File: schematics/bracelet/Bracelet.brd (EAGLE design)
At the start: 70 x 25 mm, 14 parts

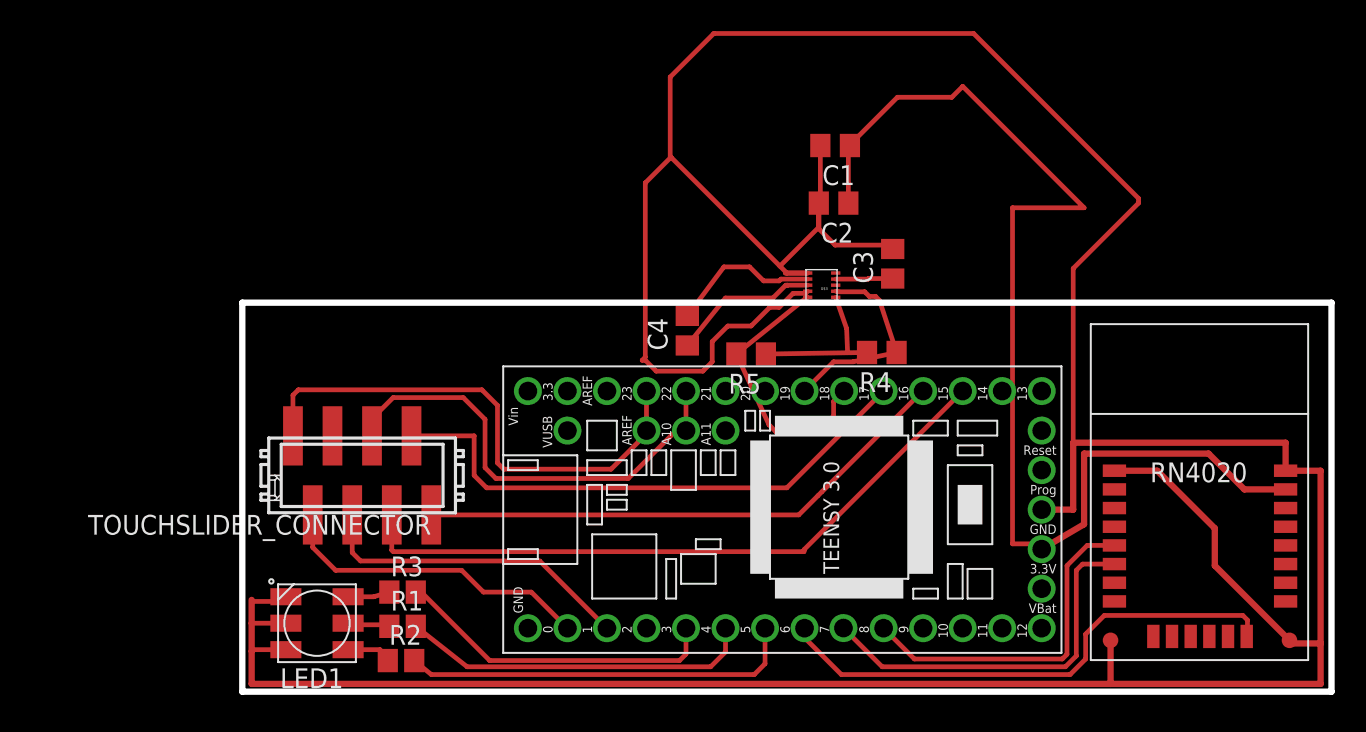
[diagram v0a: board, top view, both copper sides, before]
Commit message: finished layout, accel pullups need to be conf'ed to internal.
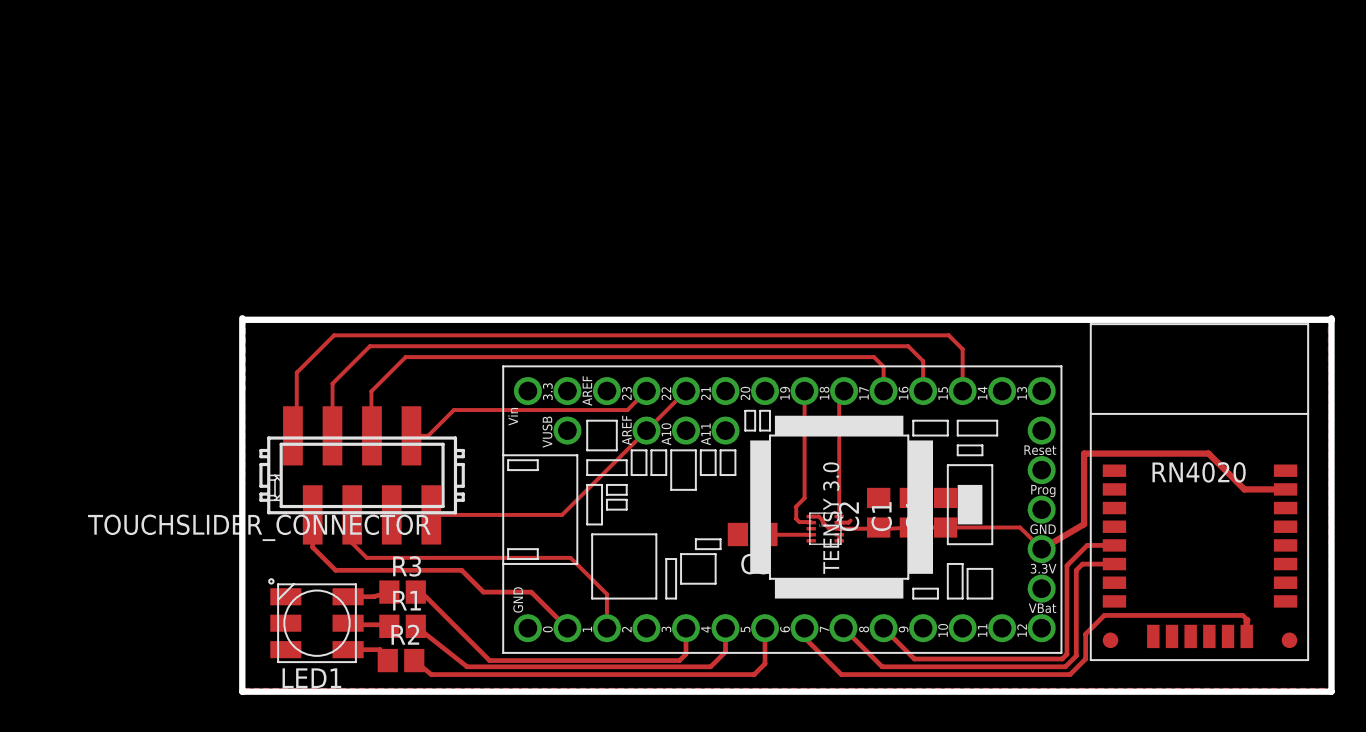
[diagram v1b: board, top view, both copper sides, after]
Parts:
- removed R4, R5: 1k, rcl:R0805
- moved C1 24.1 mm to (56.0, 36.5), turned to 90 degrees
- moved C4 20.3 mm to (58.2, 36.5)
- moved C2 20.1 mm to (53.9, 36.5), turned to 90 degrees
- moved C3 19.6 mm to (45.8, 35.1), turned to 180 degrees
- moved U$3 17.7 mm to (49.2, 34.5), turned to 0 degrees
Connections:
- removed net VDDIO: R4.2, R5.1
- net CAP01: now also U$1.P17; no longer U$1.P25
- net CAP03: now also U$1.P18
- net CAP05: now also U$1.P19; no longer U$1.P24
- net CAP06: no longer U$1.P17
- net CAP07: now also U$1.P25; no longer U$1.P19
- net CAP08: now also U$1.P24; no longer U$1.P18
- net SCL: no longer R4.1
- net SDA: no longer R5.2
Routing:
- net GND: track 265.8 -> 1.18 mm
- net +3V3: track 86.9 -> 37.7 mm
- net CAP03: track 0.00 -> 44.6 mm
- net CAP06: track 43.3 -> 0.00 mm
- net CAP07: track 35.8 -> 16.3 mm
- net CAP01: track 36.1 -> 53.6 mm
- net CAP08: track 34.9 -> 19.7 mm
- net SDA: track 17.5 -> 8.19 mm
- net CAP05: track 29.2 -> 38.5 mm
- net VDDIO: track 6.50 -> 0.00 mm
- net SCL: track 13.3 -> 9.50 mm
- net CAP04: track 20.8 -> 21.7 mm
- net N$1: track 3.69 -> 2.82 mm
- added copper zone on layer 1, net GND
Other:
- board size 70 x 25 mm -> 70 x 24 mm

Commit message: added a simple pushbutton for increased number of options. I strongly hope that we own smd 2-pin pushbuttons in stock...
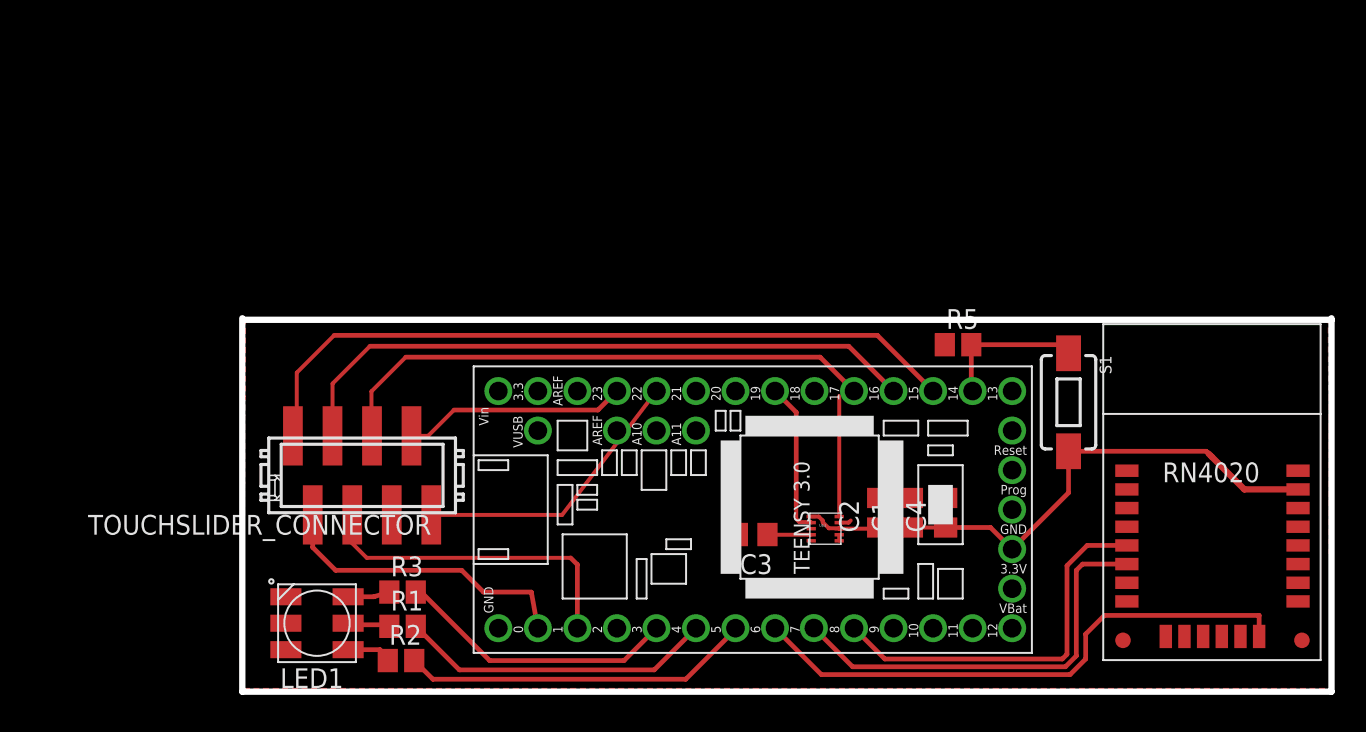
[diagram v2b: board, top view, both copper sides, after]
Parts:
- added R5: (no value), resistor:R0805
- added S1: SWITCH-MOMENTARY-2-SMD-1101NE, SparkFun-Electromechanical:TACTILE-SWITCH-1101NE
- moved U$1 1.90 mm to (46.6, 36.7)
- moved RN4020 0.80 mm to (69.6, 28.3)
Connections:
- new net N$8: R5.2, S1.1, U$1.P16
- net +3V3: now also S1.2
- net GND: now also R5.1
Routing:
- net N$8: track 0.00 -> 9.54 mm
- net CAP01: track 53.6 -> 50.2 mm
- net CAP03: track 44.6 -> 41.6 mm
- net N$7: track 25.4 -> 22.6 mm
- net N$2: track 21.0 -> 18.1 mm
- net CAP05: track 38.5 -> 35.7 mm
- net BLUETOOTH_TO_TEENSY: track 22.0 -> 24.7 mm
- net TEENSY_TO_BLUETOOTH: track 24.4 -> 27.1 mm
- net N$3: track 22.7 -> 20.3 mm
- net BLUETOOTH_WAKE_HW: track 33.8 -> 36.2 mm
- net CAP07: track 16.3 -> 14.4 mm
- net CAP08: track 19.7 -> 18.4 mm
- net CAP02: track 20.6 -> 19.7 mm
- net CAP04: track 21.7 -> 20.9 mm

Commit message: finished bracelet design and etched a board.
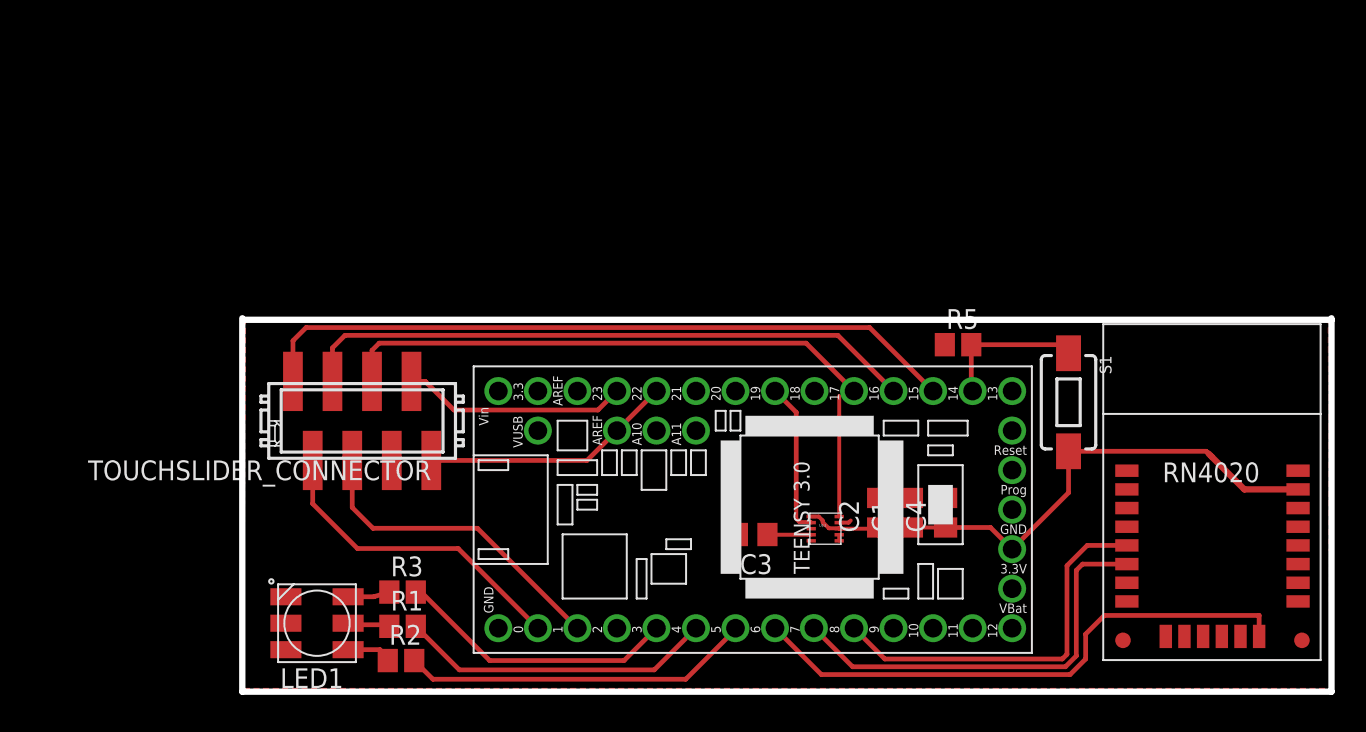
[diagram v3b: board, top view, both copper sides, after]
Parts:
- moved TOUCHSLIDER_CONNECTOR 3.50 mm to (20.7, 42.4)
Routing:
- net CAP01: track 50.2 -> 45.8 mm
- net CAP08: track 18.4 -> 16.3 mm
- net CAP03: track 41.6 -> 40.0 mm
- net CAP05: track 35.7 -> 34.4 mm
- net CAP02: track 19.7 -> 20.6 mm
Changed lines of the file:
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@@
 <element name="R2" library="resistor" package="R0805" value="" x="23.2" y="27"/>
 <element name="R3" library="resistor" package="R0805" value="" x="23.3" y="31.4"/>
-<element name="TOUCHSLIDER_CONNECTOR" library="con-amp-micromatch-smd" package="MICROMATCH-8-SMD" value="MICROMATCH-8SMD" x="20.7" y="38.9" rot="R180"/>
+<element name="TOUCHSLIDER_CONNECTOR" library="con-amp-micromatch-smd" package="MICROMATCH-8-SMD" value="MICROMATCH-8SMD" x="20.7" y="42.4" rot="R180"/>
 <element name="U$3" library="talons" package="MMA8652FC" value="MMA8652FC" x="49.2" y="34.5"/>
 <element name="C1" library="rcl" package="C0805" value="1uF" x="56" y="36.5" rot="R90"/>
@@
 <wire x1="51.965" y1="35.865" x2="52.1" y2="36" width="0.254" layer="1"/>
 <contactref element="R5" pad="1"/>
-<wire x1="51.3625" y1="35.865" x2="51.3625" y2="35.085" width="0" layer="19" extent="1-1"/>
+<wire x1="51.3625" y1="35.085" x2="51.3625" y2="35.865" width="0" layer="19" extent="1-1"/>
 </signal>
 <signal name="N$4">
@@
 <signal name="CAP01">
 <contactref element="TOUCHSLIDER_CONNECTOR" pad="1"/>
-<wire x1="16.4" y1="42.685" x2="16.255" y2="41.44" width="0.3048" layer="1"/>
-<wire x1="16.5" y1="42.785" x2="16.255" y2="41.44" width="0.3048" layer="1"/>
 <contactref element="U$1" pad="P17"/>
-<wire x1="18.9" y1="47.9" x2="16.5" y2="45.5" width="0.254" layer="1"/>
-<wire x1="16.5" y1="45.5" x2="16.5" y2="41.685" width="0.254" layer="1"/>
-<wire x1="16.5" y1="41.685" x2="16.255" y2="41.44" width="0.254" layer="1"/>
-<wire x1="18.9" y1="47.9" x2="53.815" y2="47.9" width="0.3048" layer="1"/>
-<wire x1="53.815" y1="47.9" x2="57.395" y2="44.32" width="0.3048" layer="1"/>
+<wire x1="53.315" y1="48.4" x2="57.395" y2="44.32" width="0.3048" layer="1"/>
+<wire x1="53.315" y1="48.4" x2="17.1" y2="48.4" width="0.3048" layer="1"/>
+<wire x1="17.1" y1="48.4" x2="16.255" y2="47.555" width="0.3048" layer="1"/>
+<wire x1="16.255" y1="47.555" x2="16.255" y2="44.94" width="0.3048" layer="1"/>
 </signal>
 <signal name="CAP02">
 <contactref element="TOUCHSLIDER_CONNECTOR" pad="2"/>
 <contactref element="U$1" pad="P2"/>
-<wire x1="28.5" y1="31.4" x2="31.575" y2="31.4" width="0.3048" layer="1"/>
-<wire x1="31.575" y1="31.4" x2="31.995" y2="29.08" width="0.3048" layer="1"/>
-<wire x1="17.525" y1="36.36" x2="17.525" y2="34.275" width="0.3048" layer="1"/>
-<wire x1="17.525" y1="34.275" x2="19" y2="32.8" width="0.3048" layer="1"/>
-<wire x1="19" y1="32.8" x2="27.1" y2="32.8" width="0.3048" layer="1"/>
-<wire x1="27.1" y1="32.8" x2="28.5" y2="31.4" width="0.3048" layer="1"/>
+<wire x1="31.995" y1="29.08" x2="26.875" y2="34.2" width="0.3048" layer="1"/>
+<wire x1="26.875" y1="34.2" x2="20.4" y2="34.2" width="0.3048" layer="1"/>
+<wire x1="20.4" y1="34.2" x2="17.525" y2="37.075" width="0.3048" layer="1"/>
+<wire x1="17.525" y1="37.075" x2="17.525" y2="39.86" width="0.3048" layer="1"/>
 </signal>
 <signal name="CAP03">
 <contactref element="TOUCHSLIDER_CONNECTOR" pad="3"/>
 <contactref element="U$1" pad="P18"/>
-<wire x1="21.2" y1="47.2" x2="18.8" y2="44.8" width="0.254" layer="1"/>
-<wire x1="18.8" y1="44.8" x2="18.8" y2="41.445" width="0.254" layer="1"/>
-<wire x1="18.8" y1="41.445" x2="18.795" y2="41.44" width="0.254" layer="1"/>
-<wire x1="21.2" y1="47.2" x2="51.975" y2="47.2" width="0.3048" layer="1"/>
-<wire x1="51.975" y1="47.2" x2="54.855" y2="44.32" width="0.3048" layer="1"/>
+<wire x1="51.275" y1="47.9" x2="54.855" y2="44.32" width="0.3048" layer="1"/>
+<wire x1="51.275" y1="47.9" x2="19.6" y2="47.9" width="0.3048" layer="1"/>
+<wire x1="19.6" y1="47.9" x2="18.795" y2="47.095" width="0.3048" layer="1"/>
+<wire x1="18.795" y1="47.095" x2="18.795" y2="44.94" width="0.3048" layer="1"/>
 </signal>
 <signal name="CAP04">
 <contactref element="TOUCHSLIDER_CONNECTOR" pad="4"/>
 <contactref element="U$1" pad="P3"/>
-<wire x1="34.1" y1="33.6" x2="21" y2="33.6" width="0.254" layer="1"/>
-<wire x1="21" y1="33.6" x2="20.065" y2="34.535" width="0.254" layer="1"/>
-<wire x1="20.065" y1="34.535" x2="20.065" y2="36.36" width="0.254" layer="1"/>
-<wire x1="34.1" y1="33.6" x2="34.535" y2="33.165" width="0.3048" layer="1"/>
-<wire x1="34.535" y1="33.165" x2="34.535" y2="29.08" width="0.3048" layer="1"/>
+<wire x1="34.535" y1="29.08" x2="28.115" y2="35.5" width="0.3048" layer="1"/>
+<wire x1="28.115" y1="35.5" x2="21.4" y2="35.5" width="0.3048" layer="1"/>
+<wire x1="21.4" y1="35.5" x2="20.065" y2="36.835" width="0.3048" layer="1"/>
+<wire x1="20.065" y1="36.835" x2="20.065" y2="39.86" width="0.3048" layer="1"/>
 </signal>
 <signal name="CAP05">
 <contactref element="TOUCHSLIDER_CONNECTOR" pad="5"/>
 <contactref element="U$1" pad="P19"/>
-<wire x1="23.5" y1="46.5" x2="21.3" y2="44.3" width="0.254" layer="1"/>
-<wire x1="21.3" y1="44.3" x2="21.3" y2="41.475" width="0.254" layer="1"/>
-<wire x1="21.3" y1="41.475" x2="21.335" y2="41.44" width="0.254" layer="1"/>
-<wire x1="23.5" y1="46.5" x2="50.135" y2="46.5" width="0.3048" layer="1"/>
-<wire x1="50.135" y1="46.5" x2="52.315" y2="44.32" width="0.3048" layer="1"/>
+<wire x1="49.235" y1="47.4" x2="52.315" y2="44.32" width="0.3048" layer="1"/>
+<wire x1="49.235" y1="47.4" x2="21.8" y2="47.4" width="0.3048" layer="1"/>
+<wire x1="21.8" y1="47.4" x2="21.335" y2="46.935" width="0.3048" layer="1"/>
+<wire x1="21.335" y1="46.935" x2="21.335" y2="44.94" width="0.3048" layer="1"/>
 </signal>
 <signal name="CAP06">
@@
 <contactref element="TOUCHSLIDER_CONNECTOR" pad="7"/>
 <contactref element="U$1" pad="P25"/>
-<wire x1="26.6" y1="43.1" x2="24.94" y2="41.44" width="0.254" layer="1"/>
-<wire x1="24.94" y1="41.44" x2="23.875" y2="41.44" width="0.254" layer="1"/>
 <wire x1="26.6" y1="43.1" x2="35.855" y2="43.1" width="0.3048" layer="1"/>
 <wire x1="35.855" y1="43.1" x2="37.075" y2="44.32" width="0.3048" layer="1"/>
+<wire x1="26.6" y1="43.1" x2="24.76" y2="44.94" width="0.3048" layer="1"/>
+<wire x1="24.76" y1="44.94" x2="23.875" y2="44.94" width="0.3048" layer="1"/>
 </signal>
 <signal name="CAP08">
 <contactref element="TOUCHSLIDER_CONNECTOR" pad="8"/>
 <contactref element="U$1" pad="P24"/>
-<wire x1="39.615" y1="44.32" x2="33.555" y2="36.36" width="0.254" layer="1"/>
-<wire x1="33.555" y1="36.36" x2="25.145" y2="36.36" width="0.254" layer="1"/>
+<wire x1="39.615" y1="44.32" x2="35.155" y2="39.86" width="0.3048" layer="1"/>
+<wire x1="35.155" y1="39.86" x2="25.145" y2="39.86" width="0.3048" layer="1"/>
 </signal>
 <signal name="SS">

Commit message: new bracelet version with slightly broader wires next to the accelerometer. since they always broke :(
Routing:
- net SDA: track 7.75 -> 8.72 mm
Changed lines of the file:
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@@
 <wire x1="51.965" y1="35.865" x2="52.1" y2="36" width="0.254" layer="1"/>
 <contactref element="R5" pad="1"/>
-<wire x1="51.3625" y1="35.085" x2="51.3625" y2="35.865" width="0" layer="19" extent="1-1"/>
 </signal>
 <signal name="N$4">
@@
 <contactref element="U$3" pad="P$10"/>
 <contactref element="U$1" pad="P20"/>
-<wire x1="51.3625" y1="36.255" x2="51.3625" y2="44.0075" width="0.254" layer="1"/>
-<wire x1="51.3625" y1="44.0075" x2="49.775" y2="44.32" width="0" layer="19" extent="1-1"/>
+<wire x1="51.3625" y1="36.255" x2="51.3625" y2="42.7325" width="0.3048" layer="1"/>
+<wire x1="51.3625" y1="42.7325" x2="49.775" y2="44.32" width="0.3048" layer="1"/>
 </signal>
 <signal name="SCL">
 <contactref element="U$3" pad="P$2"/>
 <contactref element="U$1" pad="P21"/>
-<wire x1="48.6" y1="36.9" x2="48.6" y2="36.1" width="0.254" layer="1"/>
 <wire x1="48.6" y1="36.1" x2="48.8" y2="35.9" width="0.254" layer="1"/>
 <wire x1="48.8" y1="35.9" x2="49.5275" y2="35.9" width="0.254" layer="1"/>
 <wire x1="49.5275" y1="35.9" x2="49.5625" y2="35.865" width="0.254" layer="1"/>
-<wire x1="48.6" y1="36.9" x2="48.6" y2="42.955" width="0.3048" layer="1"/>
+<wire x1="48.6" y1="36.1" x2="48.6" y2="42.955" width="0.3048" layer="1"/>
 <wire x1="48.6" y1="42.955" x2="47.235" y2="44.32" width="0.3048" layer="1"/>
 </signal>
